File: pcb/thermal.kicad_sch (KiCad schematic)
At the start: 0 parts

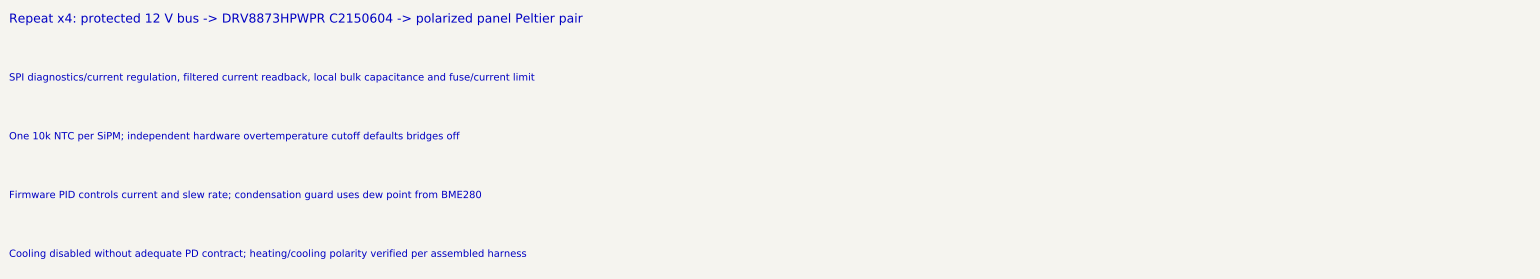
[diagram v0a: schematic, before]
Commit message: Update everything: layman summaries, Google Photos/Drive connectors for docs/sims/data/tests, multi-account support, rclone integration, enhanced pull scripts, PCB design refinements, Muon3Vision assets, 3D models, build improvements
- Added/updated layman summaries in main READMEs (physics, pcb, Muon3Vision, sim)
- Full Google Photos connector with date/keyword filtering to explore library for data and tests
- New Google Drive pull script for simulations and additional information
- Support for all accounts via separate OAuth / rclone remotes
- Installed rclone; documented connectors after system check (no desktop sync active)
- Updated scripts/, .gitignore, build_paper.sh --pull-images, main docs
- PCB architecture updates (power, DACs, hardware TEC safety, telemetry RP2040)
- Added missing part READMEs and 3D models
- Muon3Vision resources and Package.swift

All changes documented and ready for use.
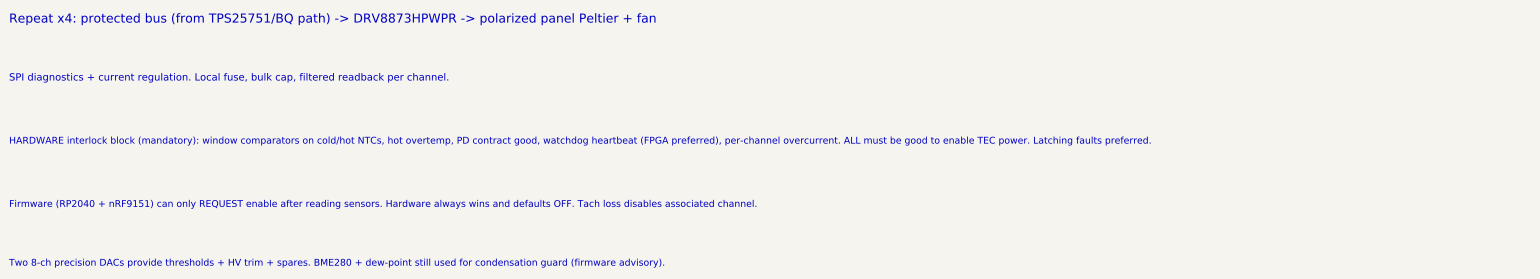
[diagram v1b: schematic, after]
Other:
- note added: "Firmware (RP2040 + nRF9151) can only REQUEST enable after reading sensors. Hardware always wins and defaults OFF. Tach loss disables associated channel."
- note added: "HARDWARE interlock block (mandatory): window comparators on cold/hot NTCs, hot overtemp, PD contract good, watchdog heartbeat (FPGA preferred), per-channel overcurrent. ALL must be good to enable TEC power. Latching faults preferred."
- note added: "Repeat x4: protected bus (from TPS25751/BQ path) -> DRV8873HPWPR -> polarized panel Peltier + fan"
- note added: "SPI diagnostics + current regulation. Local fuse, bulk cap, filtered readback per channel."
- note added: "Two 8-ch precision DACs provide thresholds + HV trim + spares. BME280 + dew-point still used for condensation guard (firmware advisory)."
- note removed: "Cooling disabled without adequate PD contract; heating/cooling polarity verified per assembled harness"
- note removed: "Firmware PID controls current and slew rate; condensation guard uses dew point from BME280"
- note removed: "One 10k NTC per SiPM; independent hardware overtemperature cutoff defaults bridges off"
- note removed: "Repeat x4: protected 12 V bus -> DRV8873HPWPR C2150604 -> polarized panel Peltier pair"
- note removed: "SPI diagnostics/current regulation, filtered current readback, local bulk capacitance and fuse/current limit"
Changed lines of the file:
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@@
  (paper "A3")
   (title_block (title "Muon3 Peltier and temperature control") (date "2026-07-11") (rev "P0") (comment 1 "ARCHITECTURE - electrical capture pending"))
-  (text "Repeat x4: protected 12 V bus -> DRV8873HPWPR C2150604 -> polarized panel Peltier pair" (at 25 35 0) (effects (font (size 2 2)) (justify left)))
-  (text "SPI diagnostics/current regulation, filtered current readback, local bulk capacitance and fuse/current limit" (at 25 48 0) (effects (font (size 1.6 1.6)) (justify left)))
-  (text "One 10k NTC per SiPM; independent hardware overtemperature cutoff defaults bridges off" (at 25 61 0) (effects (font (size 1.6 1.6)) (justify left)))
-  (text "Firmware PID controls current and slew rate; condensation guard uses dew point from BME280" (at 25 74 0) (effects (font (size 1.6 1.6)) (justify left)))
-  (text "Cooling disabled without adequate PD contract; heating/cooling polarity verified per assembled harness" (at 25 87 0) (effects (font (size 1.6 1.6)) (justify left)))
+  (text "Repeat x4: protected bus (from TPS25751/BQ path) -> DRV8873HPWPR -> polarized panel Peltier + fan" (at 25 35 0) (effects (font (size 2 2)) (justify left)))
+  (text "SPI diagnostics + current regulation. Local fuse, bulk cap, filtered readback per channel." (at 25 48 0) (effects (font (size 1.6 1.6)) (justify left)))
+  (text "HARDWARE interlock block (mandatory): window comparators on cold/hot NTCs, hot overtemp, PD contract good, watchdog heartbeat (FPGA preferred), per-channel overcurrent. ALL must be good to enable TEC power. Latching faults preferred." (at 25 62 0) (effects (font (size 1.5 1.5)) (justify left)))
+  (text "Firmware (RP2040 + nRF9151) can only REQUEST enable after reading sensors. Hardware always wins and defaults OFF. Tach loss disables associated channel." (at 25 76 0) (effects (font (size 1.5 1.5)) (justify left)))
+  (text "Two 8-ch precision DACs provide thresholds + HV trim + spares. BME280 + dew-point still used for condensation guard (firmware advisory)." (at 25 89 0) (effects (font (size 1.5 1.5)) (justify left)))
   (sheet_instances (path "/" (page "5"))) (embedded_fonts no)
 )

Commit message: Update paper with latest architecture, add openEMS EM simulations (RF, SI, PDN), update schematics with real symbols/wires, add 3D models and openEMS figures
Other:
- note removed: "Firmware (RP2040 + nRF9151) can only REQUEST enable after reading sensors. Hardware always wins and defaults OFF. Tach loss disables associated channel."
- note removed: "HARDWARE interlock block (mandatory): window comparators on cold/hot NTCs, hot overtemp, PD contract good, watchdog heartbeat (FPGA preferred), per-channel overcurrent. ALL must be good to enable TEC power. Latching faults preferred."
- note removed: "Repeat x4: protected bus (from TPS25751/BQ path) -> DRV8873HPWPR -> polarized panel Peltier + fan"
- note removed: "SPI diagnostics + current regulation. Local fuse, bulk cap, filtered readback per channel."
- note removed: "Two 8-ch precision DACs provide thresholds + HV trim + spares. BME280 + dew-point still used for condensation guard (firmware advisory)."
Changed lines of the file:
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@@
-(kicad_sch (version 20250114) (generator "eeschema") (generator_version "9.0")
- (paper "A3")
-  (title_block (title "Muon3 Peltier and temperature control") (date "2026-07-11") (rev "P0") (comment 1 "ARCHITECTURE - electrical capture pending"))
-  (text "Repeat x4: protected bus (from TPS25751/BQ path) -> DRV8873HPWPR -> polarized panel Peltier + fan" (at 25 35 0) (effects (font (size 2 2)) (justify left)))
-  (text "SPI diagnostics + current regulation. Local fuse, bulk cap, filtered readback per channel." (at 25 48 0) (effects (font (size 1.6 1.6)) (justify left)))
-  (text "HARDWARE interlock block (mandatory): window comparators on cold/hot NTCs, hot overtemp, PD contract good, watchdog heartbeat (FPGA preferred), per-channel overcurrent. ALL must be good to enable TEC power. Latching faults preferred." (at 25 62 0) (effects (font (size 1.5 1.5)) (justify left)))
-  (text "Firmware (RP2040 + nRF9151) can only REQUEST enable after reading sensors. Hardware always wins and defaults OFF. Tach loss disables associated channel." (at 25 76 0) (effects (font (size 1.5 1.5)) (justify left)))
-  (text "Two 8-ch precision DACs provide thresholds + HV trim + spares. BME280 + dew-point still used for condensation guard (firmware advisory)." (at 25 89 0) (effects (font (size 1.5 1.5)) (justify left)))
-  (sheet_instances (path "/" (page "5"))) (embedded_fonts no)
+(kicad_sch
+	(version 20260306)
+	(generator "eeschema")
+	(generator_version "10.0")
+	(paper "A3")
+	(title_block
+		(title "Muon3 Peltier and temperature control")
+		(date "2026-07-11")
+		(rev "P1")
+		(comment 1 "BASIC SCHEMATIC - WIP")
+	)
 )
